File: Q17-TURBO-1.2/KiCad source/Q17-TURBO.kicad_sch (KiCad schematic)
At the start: 93 parts, among them J1 INPUT, J2 SPK+, J3 DC, Q1 IRF610, Q10 KSA992, Q12 KSC1845, Q13 IRF610, Q14 IRF9610, Q15 FQA46N15, Q16 IXTH48P20P, Q17 FQA46N15, Q18 IXTH48P20P, Q2 KSA992, Q3 KSC1845, Q4 IRF9610, Q5 FQPF7P20, Q6 2SK3564, Q7 LSK170B, Q8 DN2540, Q9 BS250P, U1 OPA1611, U2 NDC7003P

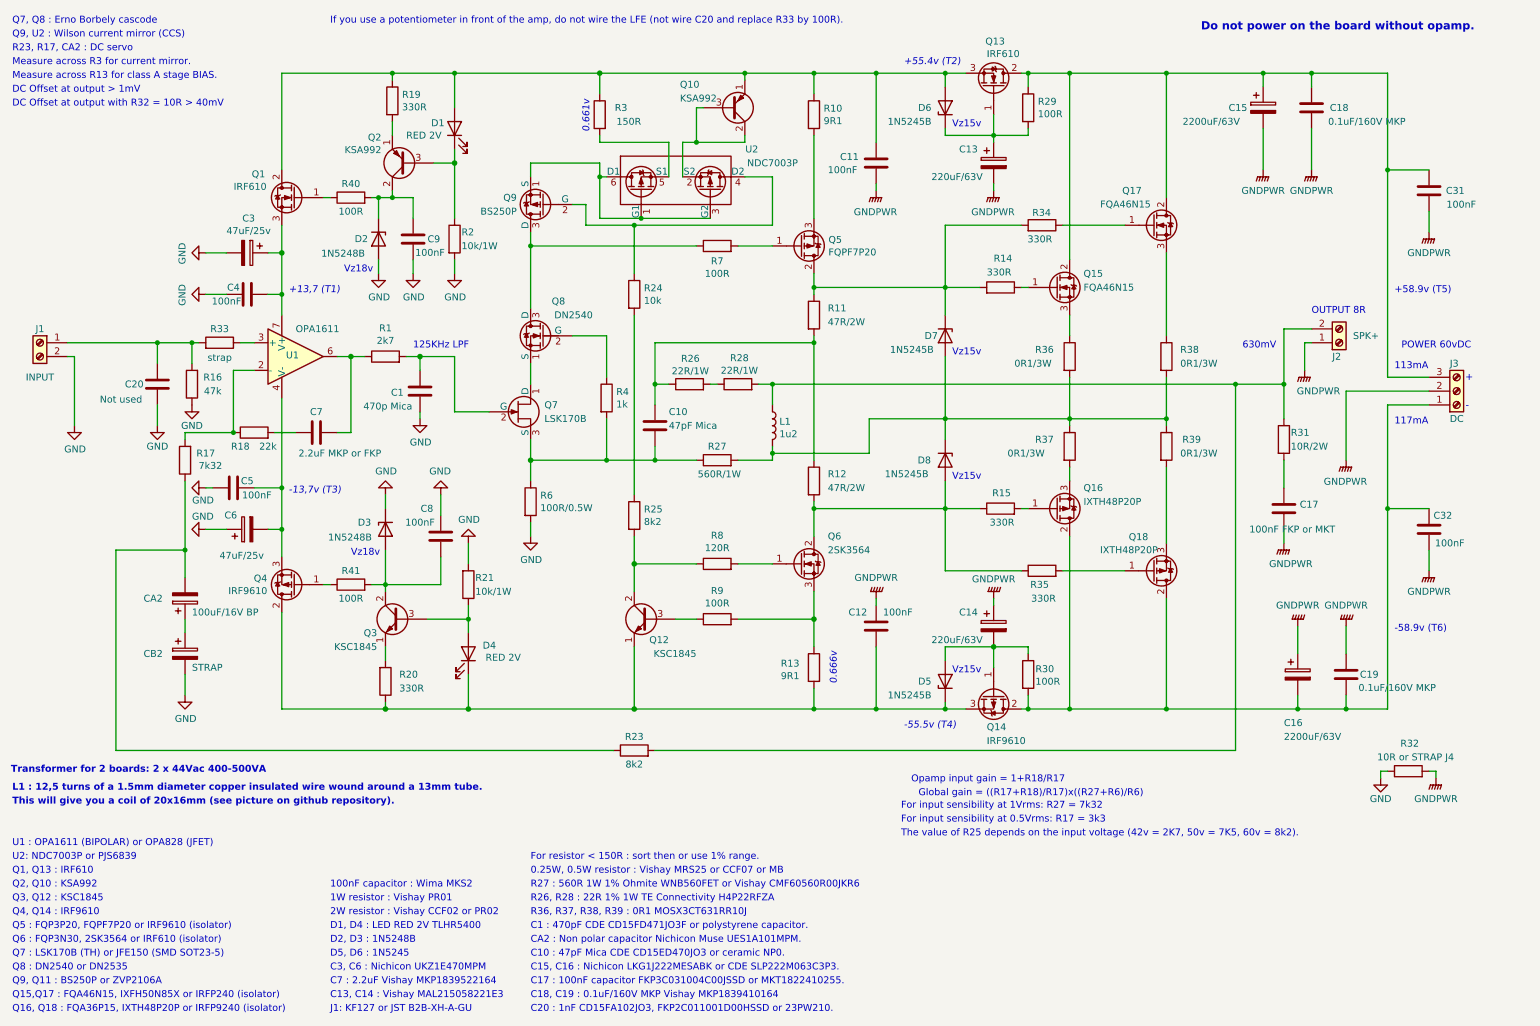
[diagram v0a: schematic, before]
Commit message: Update Q17-Turbo diagram
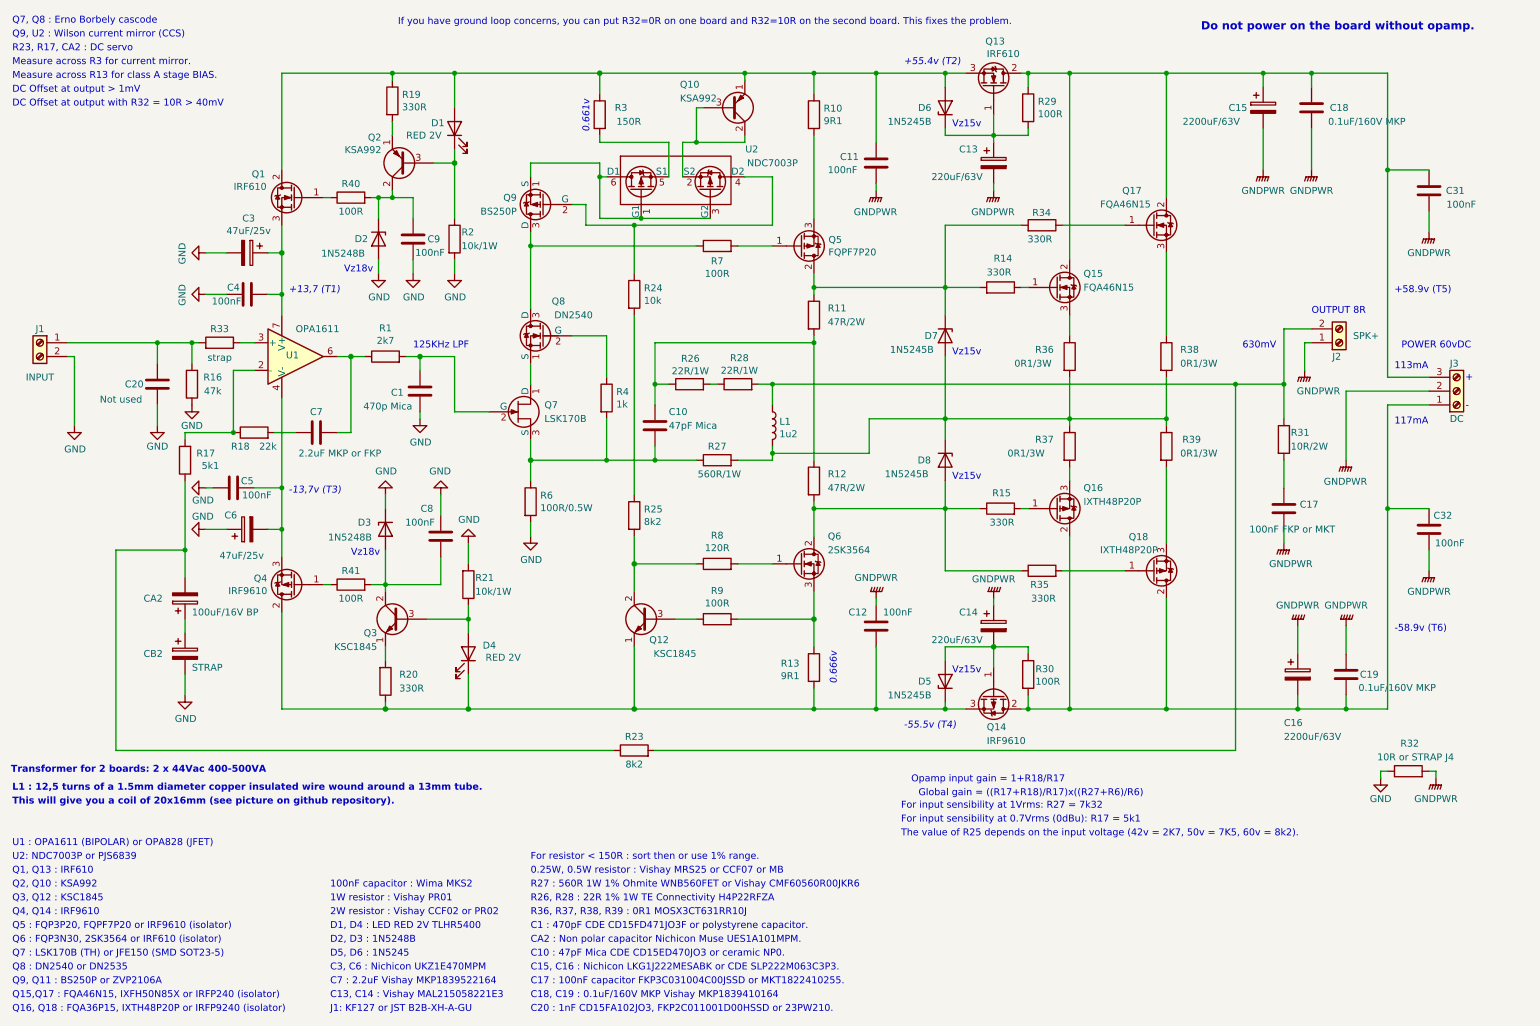
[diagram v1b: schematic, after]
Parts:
- R17: value 7k32 -> 5k1; Mouser 660-MF1/4CCT52R7321F -> 594-MRS25000C5101FRP; Part# MF1/4CCT52R7321F -> MRS25000C5101FRP00
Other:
- note added: "For input sensibility at 0.7Vrms (0dBu): R17 = 5k1"
- note added: "If you have ground loop concerns, you can put R32=0R on one board and R32=10R on the second board. This fixes the problem."
- note removed: "For input sensibility at 0.5Vrms: R17 = 3k3"
- note removed: "If you use a potentiometer in front of the amp, do not wire the LFE (not wire C20 and replace R33 by 100R)."
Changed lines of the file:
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@@
 	(title_block
 		(title "Q17-TURBO (P2) Amplifier")
-		(date "2024-05-21")
-		(rev "1.3.1")
+		(date "2024-05-27")
+		(rev "1.3.2")
 		(company "by eng. Tiberiu Vicol")
 		(comment 1 "Modified by Stef for the Q17-TURBO project")
@@
 		)
 	)
+	(text "If you have ground loop concerns, you can put R32=0R on one board and R32=10R on the second board. This fixes the problem."
+		(exclude_from_sim no)
+		(at 84.836 15.494 0)
+		(effects
+			(font
+				(size 1.27 1.27)
+			)
+			(justify left bottom)
+		)
+	)
 	(text "The value of R25 depends on the input voltage (42v = 2K7, 50v = 7K5, 60v = 8k2)."
 		(exclude_from_sim no)
@@
 		)
 	)
-	(text "For input sensibility at 0.5Vrms: R17 = 3k3"
+	(text "For input sensibility at 0.7Vrms (0dBu): R17 = 5k1"
 		(exclude_from_sim no)
 		(at 177.292 162.052 0)
@@
 		)
 	)
-	(text "If you use a potentiometer in front of the amp, do not wire the LFE (not wire C20 and replace R33 by 100R)."
-		(exclude_from_sim no)
-		(at 72.39 15.24 0)
-		(effects
-			(font
-				(size 1.27 1.27)
-			)
-			(justify left bottom)
-		)
-	)
 	(text "Q6 : FQP3N30, 2SK3564 or IRF610 (isolator)"
 		(exclude_from_sim no)
@@
 			)
 		)
-		(property "Value" "7k32"
+		(property "Value" "5k1"
 			(at 50.3802 96.2595 0)
 			(effects
@@
 			)
 		)
-		(property "Datasheet" "https://www.mouser.fr/datasheet/2/219/MF_MFS_RK-18760.pdf"
+		(property "Datasheet" "https://www.vishay.com/doc?28724"
 			(at 45.72 95.25 0)
 			(effects
@@
 			)
 		)
-		(property "Part#" "MF1/4CCT52R7321F"
+		(property "Part#" "MRS25000C5101FRP00"
 			(at 45.72 95.25 0)
 			(effects
@@
 			)
 		)
-		(property "Mouser" "660-MF1/4CCT52R7321F"
+		(property "Mouser" "594-MRS25000C5101FRP"
 			(at 45.72 95.25 0)
 			(effects

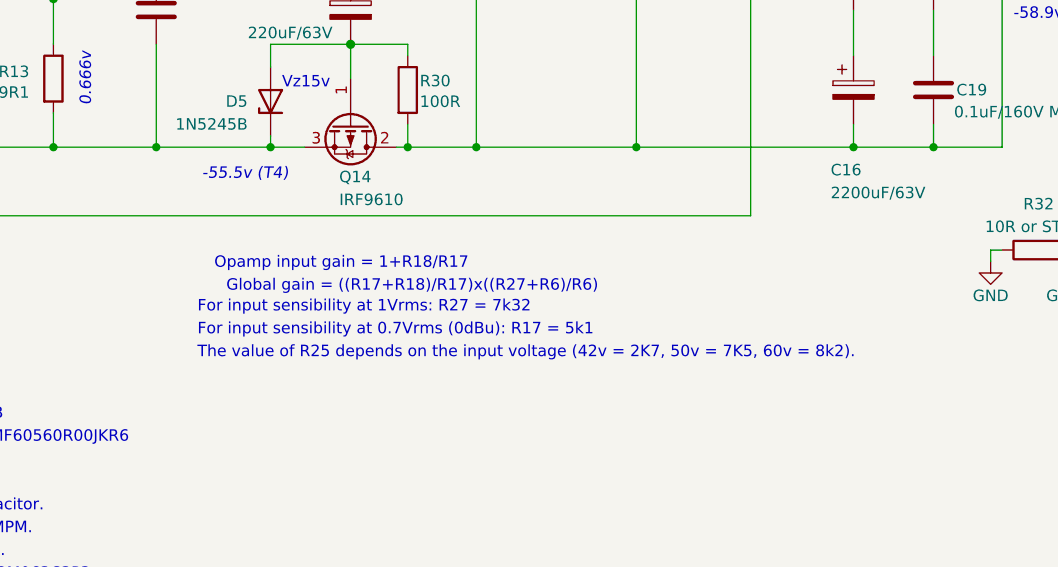
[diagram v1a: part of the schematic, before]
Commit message: Update Q17-Turbo diagram
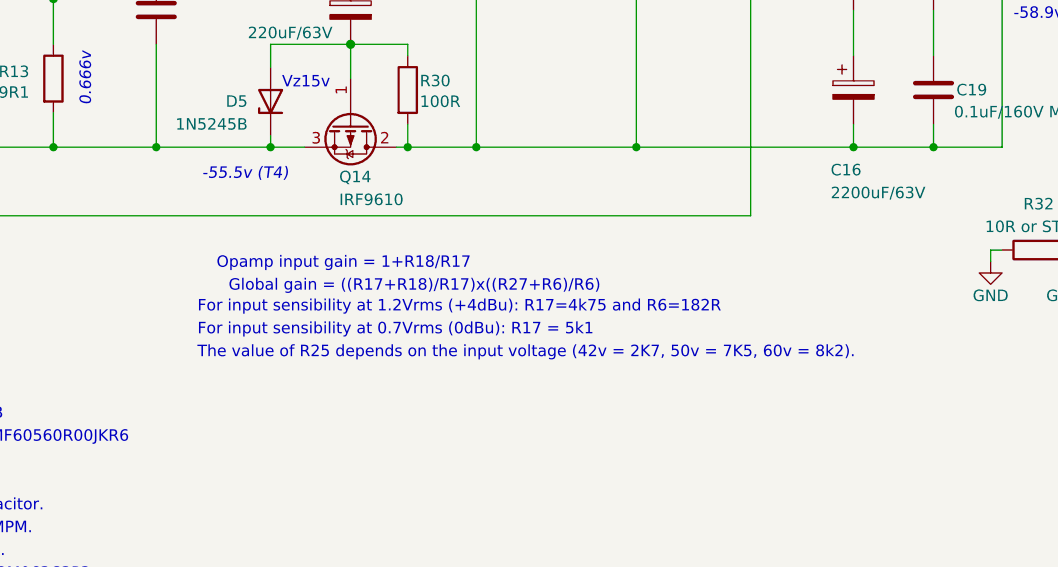
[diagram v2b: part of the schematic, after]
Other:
- note added: "For input sensibility at 1.2Vrms (+4dBu): R17=4k75 and R6=182R"
- note removed: "For input sensibility at 1Vrms: R27 = 7k32"
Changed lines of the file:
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@@
 	(title_block
 		(title "Q17-TURBO (P2) Amplifier")
-		(date "2024-05-27")
-		(rev "1.3.2")
+		(date "2024-05-28")
+		(rev "1.3.3")
 		(company "by eng. Tiberiu Vicol")
 		(comment 1 "Modified by Stef for the Q17-TURBO project")
@@
 	(text "Opamp input gain = 1+R18/R17"
 		(exclude_from_sim no)
-		(at 193.294 153.924 0)
+		(at 193.548 153.924 0)
 		(effects
 			(font
@@
 		)
 	)
-	(text "For input sensibility at 1Vrms: R27 = 7k32"
-		(exclude_from_sim no)
-		(at 177.292 159.512 0)
-		(effects
-			(font
-				(size 1.27 1.27)
-			)
-			(justify left bottom)
-		)
-	)
 	(text "-"
 		(exclude_from_sim no)
@@
 		)
 	)
+	(text "For input sensibility at 1.2Vrms (+4dBu): R17=4k75 and R6=182R"
+		(exclude_from_sim no)
+		(at 177.292 159.512 0)
+		(effects
+			(font
+				(size 1.27 1.27)
+			)
+			(justify left bottom)
+		)
+	)
 	(text "D2, D3 : 1N5248B"
 		(exclude_from_sim no)
@@
 	(text "Global gain = ((R17+R18)/R17)x((R27+R6)/R6)"
 		(exclude_from_sim no)
-		(at 201.168 156.464 0)
+		(at 201.422 156.464 0)
 		(effects
 			(font

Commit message: Update Q17-Turbo files
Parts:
- R17: value 5k1 -> 4k75; Mouser 594-MRS25000C5101FRP -> 594-MRS25000C4751FRP; Part# MRS25000C5101FRP00 -> MRS25000C4751FRP00
- R6: value 100R/0.5W -> 196R/0.5W; Mouser 594-MRS25000C1000FCT -> 594-MRS25000C1960FCT; Part# MRS25000C1000FCT00 -> MRS25000C1960FCT00
- R8: value 120R -> 100R; Mouser 594-MRS25000C1200FCT -> 594-MRS25000C1000FCT; Part# MRS25000C1200FCT00 -> MRS25000C1000FCT00
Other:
- note added: "Board consumption per voltage rail without power transistors: 10mA"
- note added: "For input sensibility at 0.7Vrms (0dBu): R17 = 5k1 and R6=100R"
- note added: "For input sensibility at 1.2Vrms (+4dBu): R17=4k75 and R6=196R"
- note added: "You may need to pair Q11 and Q11 transistors to have same Vbe or Vgs at 5mA. This improves the accuracy of the CCS+ current mirror."
- note removed: "For input sensibility at 0.7Vrms (0dBu): R17 = 5k1"
- note removed: "For input sensibility at 1.2Vrms (+4dBu): R17=4k75 and R6=182R"
- note removed: "If you have ground loop concerns, you can put R32=0R on one board and R32=10R on the second board. This fixes the problem."
